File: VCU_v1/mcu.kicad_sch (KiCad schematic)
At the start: 35 parts, among them J2 NUCLEO CONNECTOR LEFT, J3 NUCLEO CONNECTOR RIGHT, SW1 SW_Push, U5 STM32H723ZGT6, Y1 16 MHz, Y2 32.768 kHz

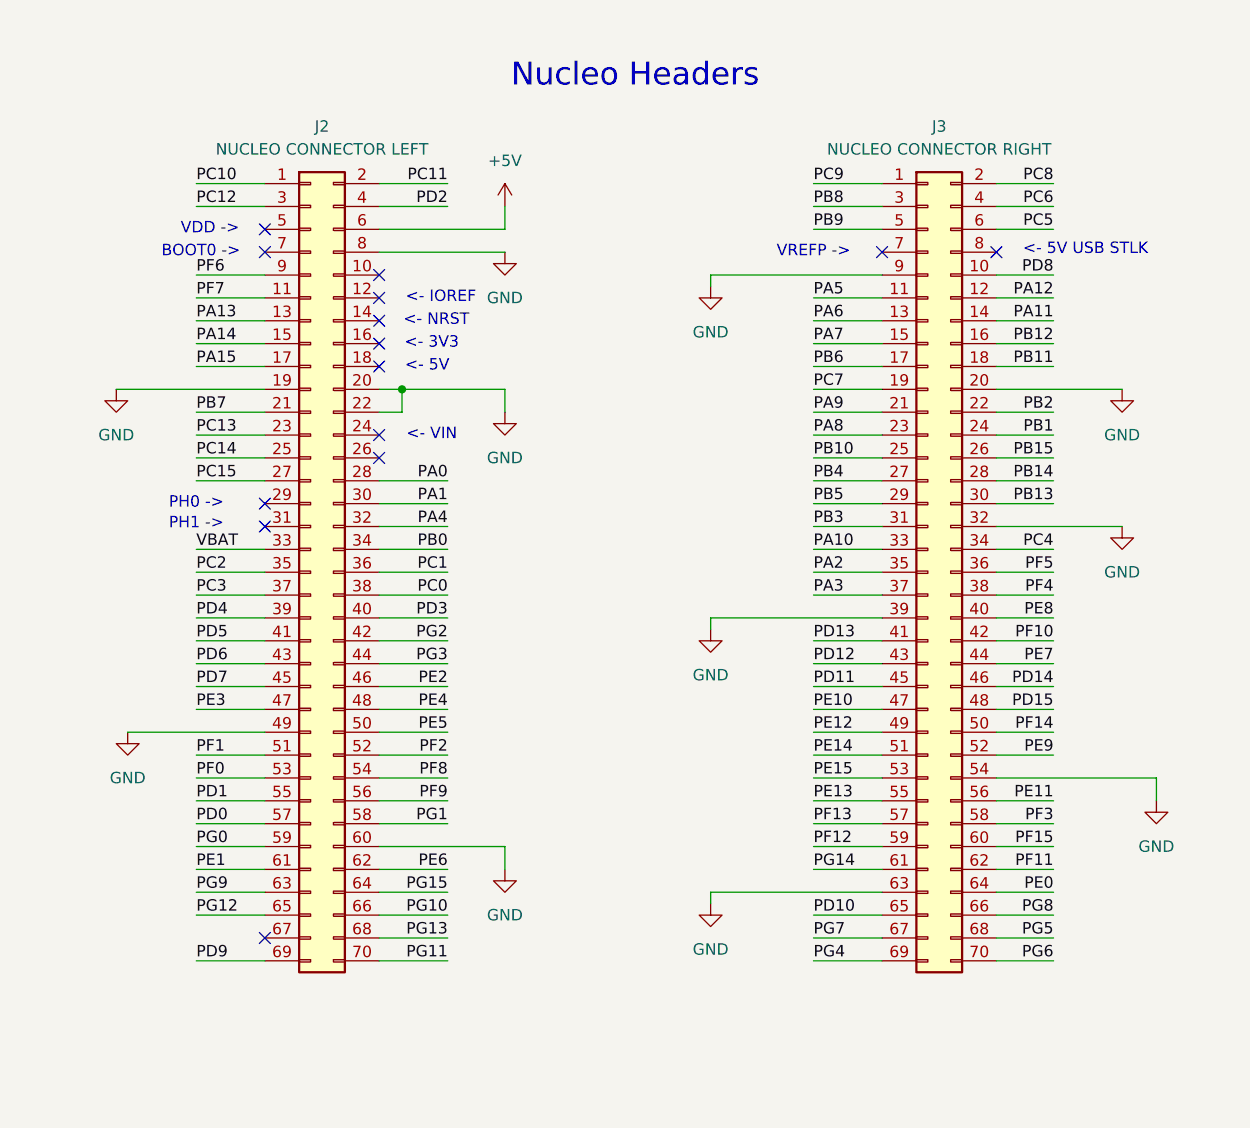
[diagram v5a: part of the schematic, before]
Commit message: fixing drc errors, done besides that
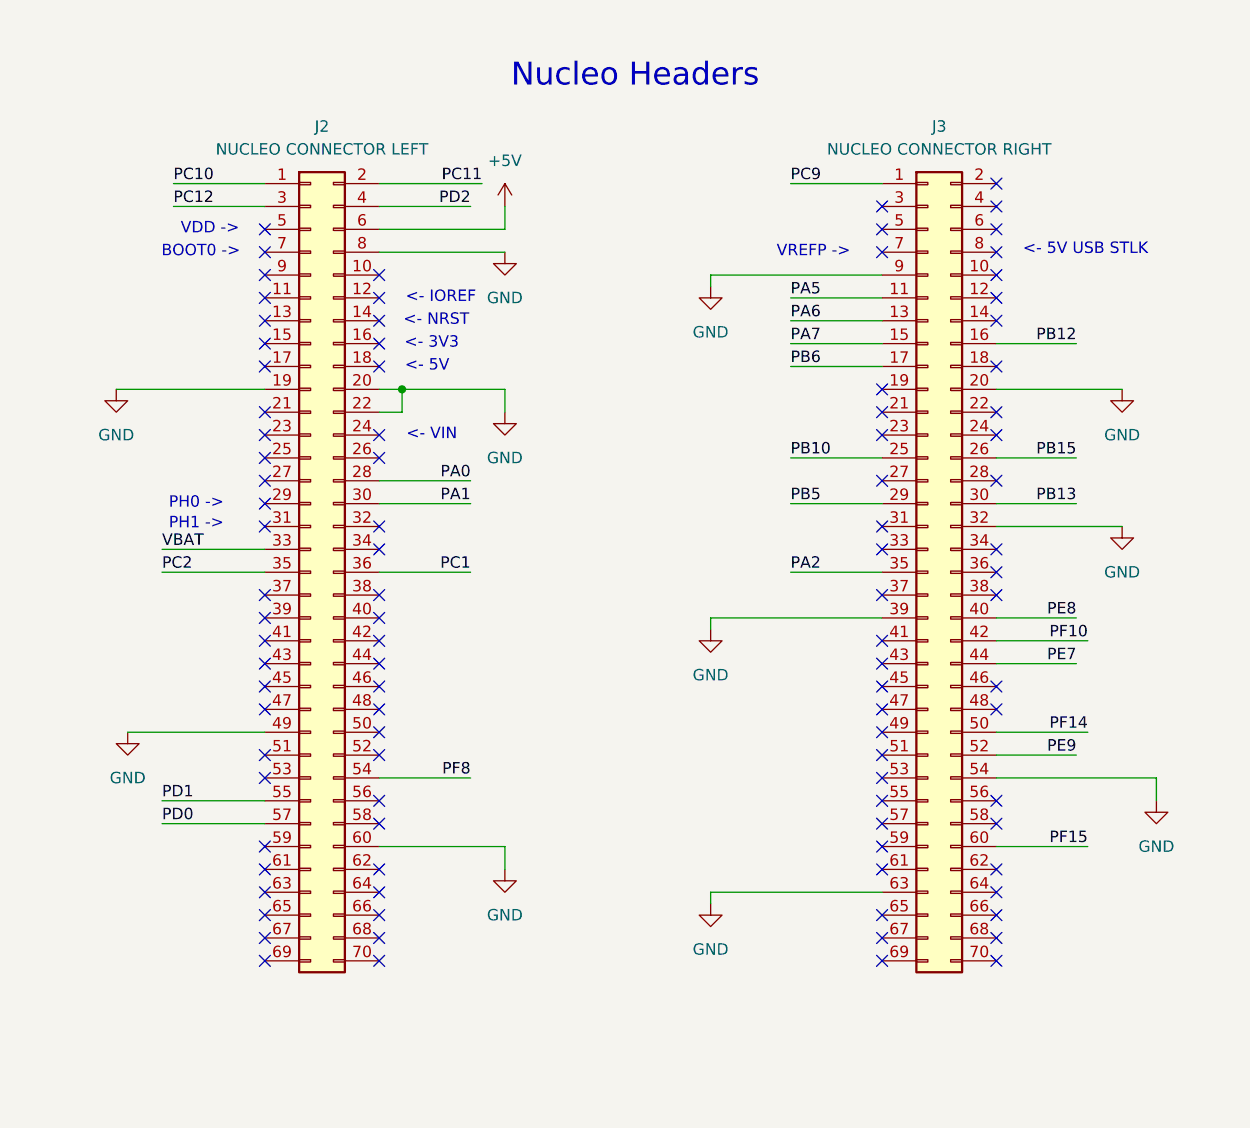
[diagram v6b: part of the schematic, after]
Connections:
- net ADC3-IN8: no longer J2.9 (Pin_9)
- net ADC3-IN9: no longer J3.38 (Pin_38)
- net DEBUG_SWCLK: no longer J2.15 (Pin_15)
- net DEBUG_SWDIO: no longer J2.13 (Pin_13)
- net DEBUG_SWO: no longer J3.31 (Pin_31)
- net FDCAN3_RX: no longer J3.43 (Pin_43)
- net FDCAN3_TX: no longer J3.41 (Pin_41)
- net GPIO_E10: no longer J3.47 (Pin_47)
- net GPIO_E11: no longer J3.56 (Pin_56)
- net GPIO_G10: no longer J2.66 (Pin_66)
- net GPIO_G11: no longer J2.70 (Pin_70)
- net GPIO_G12: no longer J2.65 (Pin_65)
- net GPIO_G13: no longer J2.68 (Pin_68)
- net GPIO_G14: no longer J3.61 (Pin_61)
- net GPIO_G15: no longer J2.64 (Pin_64)
- net GPIO_G2: no longer J2.42 (Pin_42)
- net GPIO_G3: no longer J2.44 (Pin_44)
- net GPIO_G4: no longer J3.69 (Pin_69)
- net GPIO_G5: no longer J3.68 (Pin_68)
- net GPIO_G6: no longer J3.70 (Pin_70)
- net GPIO_G7: no longer J3.67 (Pin_67)
- net GPIO_G8: no longer J3.66 (Pin_66)
- net GPIO_G9: no longer J2.63 (Pin_63)
- net GPIO_IN_F13: no longer J3.57 (Pin_57)
- net GPIO_IN_G0: no longer J2.59 (Pin_59)
- net GPIO_IN_G1: no longer J2.58 (Pin_58)
- net GPIO_OUT_E12: no longer J3.49 (Pin_49)
- net GPIO_OUT_E13: no longer J3.55 (Pin_55)
- net GPIO_OUT_E14: no longer J3.51 (Pin_51)
- net GPIO_OUT_E15: no longer J3.53 (Pin_53)
- net PA10: no longer J3.33 (Pin_33)
- net PA15: no longer J2.17 (Pin_17)
- net PA3: no longer J3.37 (Pin_37)
- net PA4: no longer J2.32 (Pin_32)
- net PA8: no longer J3.23 (Pin_23)
- net PA9: no longer J3.21 (Pin_21)
- net PB0: no longer J2.34 (Pin_34)
- net PB1: no longer J3.24 (Pin_24)
- net PB11: no longer J3.18 (Pin_18)
- net PB14: no longer J3.28 (Pin_28)
- net PB2: no longer J3.22 (Pin_22)
- net PB4: no longer J3.27 (Pin_27)
- net PB7: no longer J2.21 (Pin_21)
- net PB8: no longer J3.3 (Pin_3)
- net PB9: no longer J3.5 (Pin_5)
- net PC0: no longer J2.38 (Pin_38)
- net PC13: no longer J2.23 (Pin_23)
- net PC3: no longer J2.37 (Pin_37)
- net PC4: no longer J3.34 (Pin_34)
- net PC5: no longer J3.6 (Pin_6)
- net PC6: no longer J3.4 (Pin_4)
- net PC7: no longer J3.19 (Pin_19)
- net PC8: no longer J3.2 (Pin_2)
- net PD10: no longer J3.65 (Pin_65)
- net PD11: no longer J3.45 (Pin_45)
- net PD14: no longer J3.46 (Pin_46)
- net PD15: no longer J3.48 (Pin_48)
- net PD3: no longer J2.40 (Pin_40)
- net PD4: no longer J2.39 (Pin_39)
- net PD5: no longer J2.41 (Pin_41)
- net PD6: no longer J2.43 (Pin_43)
- net PD7: no longer J2.45 (Pin_45)
- net PD8: no longer J3.10 (Pin_10)
- net PD9: no longer J2.69 (Pin_69)
- net PE0: no longer J3.64 (Pin_64)
- net PE1: no longer J2.61 (Pin_61)
- net PE2: no longer J2.46 (Pin_46)
- net PE3: no longer J2.47 (Pin_47)
- net PE4: no longer J2.48 (Pin_48)
- net PE5: no longer J2.50 (Pin_50)
- net PE6: no longer J2.62 (Pin_62)
- net PF0: no longer J2.53 (Pin_53)
- net PF1: no longer J2.51 (Pin_51)
- net PF11: no longer J3.62 (Pin_62)
- net PF12: no longer J3.59 (Pin_59)
- net PF2: no longer J2.52 (Pin_52)
- net PF3: no longer J3.58 (Pin_58)
- net PF5: no longer J3.36 (Pin_36)
- net PF7: no longer J2.11 (Pin_11)
- net PF9: no longer J2.56 (Pin_56)
- net USB_D+: no longer J3.12 (Pin_12)
- net USB_D-: no longer J3.14 (Pin_14)
- net PC14: no longer names the net of J2.25 (Pin_25)
- net PC15: no longer names the net of J2.27 (Pin_27)
- no-connect marks 15 -> 99
